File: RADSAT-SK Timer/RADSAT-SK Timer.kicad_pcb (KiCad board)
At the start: 2 copper layers, 90.2 x 95.9 mm, 107 parts, among them J101 Conn_02x26_Odd_Even, J103 Conn_02x26_Odd_Even, J201 Conn_01x07, J202 Conn_01x05, J203 Conn_01x02, J204 Conn_01x02, J205 Conn_01x02, J206 Conn_01x02, J210 ZX62WRD-B-5PC, Q101 IRLML2060, Q102 IRLML2060, Q103 IRLML2060, Q104 IRLML2060, Q105 IRLML2060, Q106 IRLML2060, Q107 IRLML2060, Q108 IRLML2060, Q109 IRLML2060, Q201 IRLML2060, Q202 IRLML2060, SW201 SW_Push, SW202 SW_Push, SW203 SW_Push, SW204 SW_Push, SW205 SW_Push, SW206 SW_Push, U101 LM397MF, U102 LM397MF, U103 LM397MF, U104 CD4052B, U202 LTC3440EMSPBF

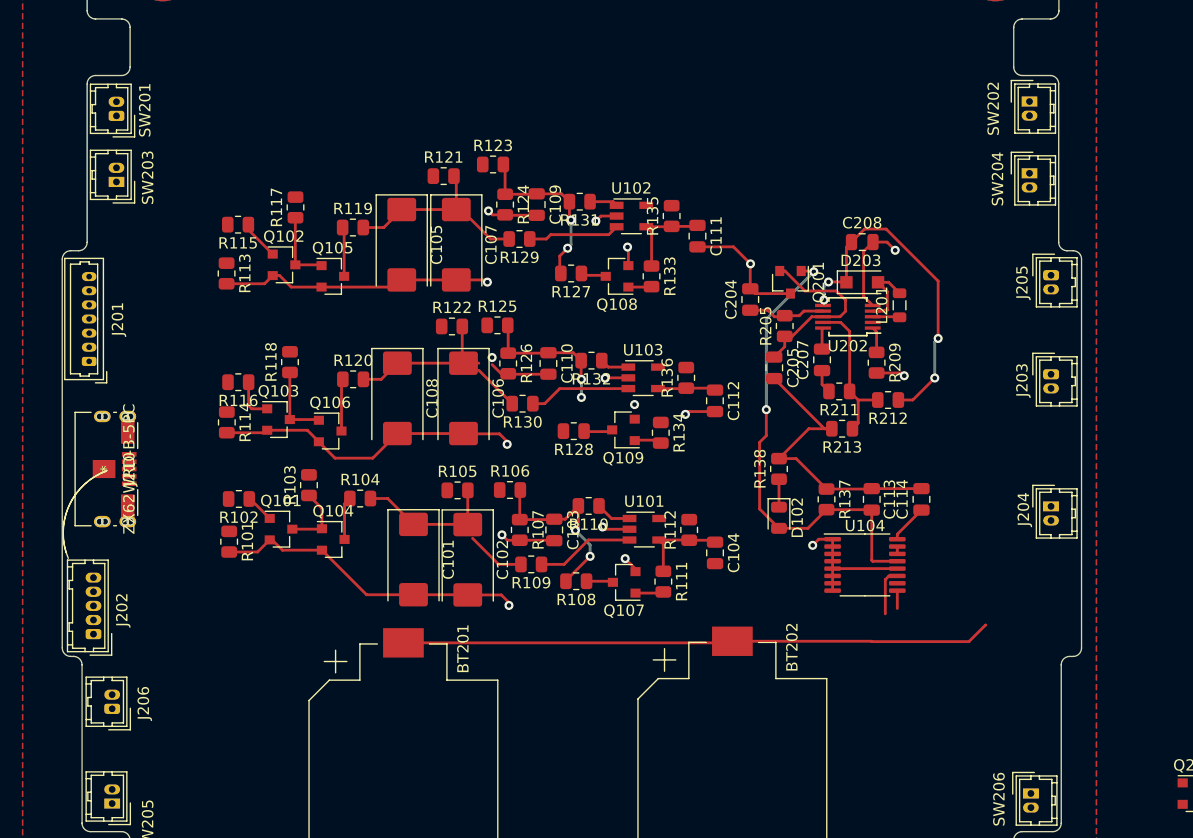
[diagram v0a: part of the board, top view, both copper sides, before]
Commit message: Cleaned Up the USb footprint and updated the libraries to play nice with KiCad
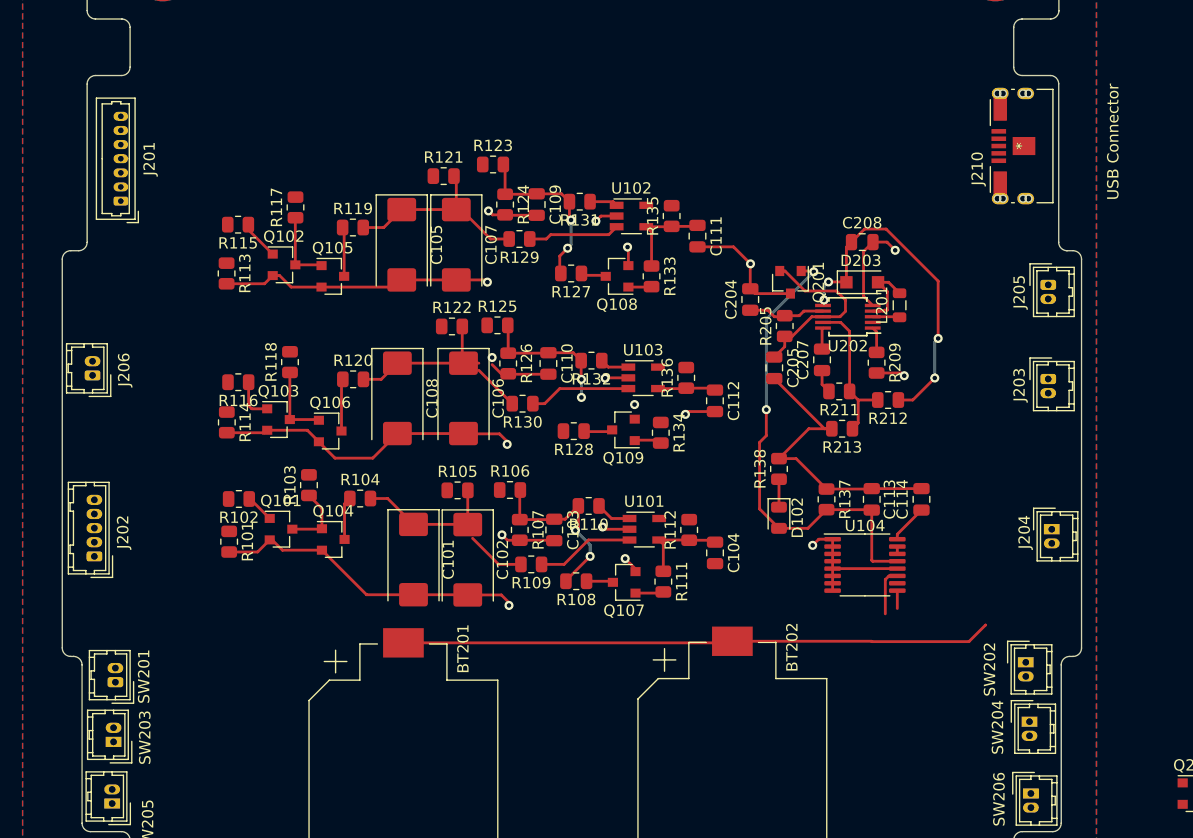
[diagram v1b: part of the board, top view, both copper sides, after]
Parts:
- C205: value C -> 0.1uF
- J210: value ZX62WRD-B-5PC -> USB Connector; footprint ZX62WRD-B-5PC:ZX62WRD-B-5PC -> CONN_ZX62WRD-B-5PC_HIR:CONN_ZX62WRD-B-5PC_HIR
- moved J210 85.9 mm to (119.7, 70.7), turned to 90 degrees
- moved SW201 50.1 mm to (39.5, 118.2)
- moved SW202 49.6 mm to (120.1, 116.4)
- moved SW203 49.5 mm to (39.4, 123.5)
- moved SW204 48.5 mm to (120.4, 121.7)
- moved J206 29.5 mm to (37.5, 91.0)
- moved J201 14.5 mm to (40.0, 75.6)
- moved J202 6.88 mm to (37.7, 107.0)
- moved J204 2.03 mm to (122.4, 104.6)
- moved J205 0.89 mm to (122.0, 83.0)
- moved J203 0.49 mm to (122.0, 91.3)

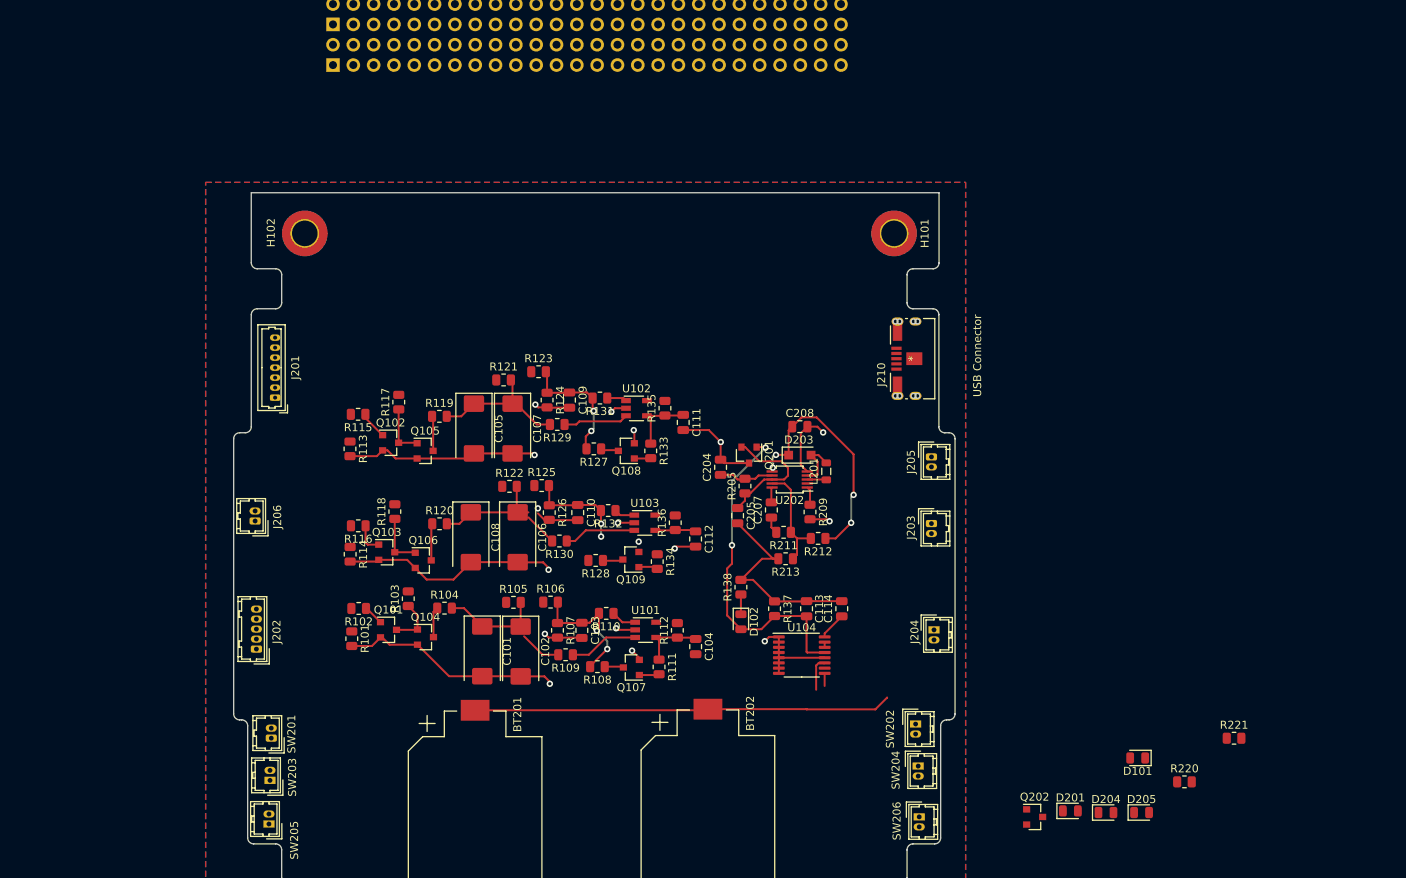
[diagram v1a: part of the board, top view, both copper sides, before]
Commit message: More Library management, added text to pcb to identify easily connectors, Added a cool custom USST RADSAT-SK Logo to the project, may need to be scaled down or placed on back of board
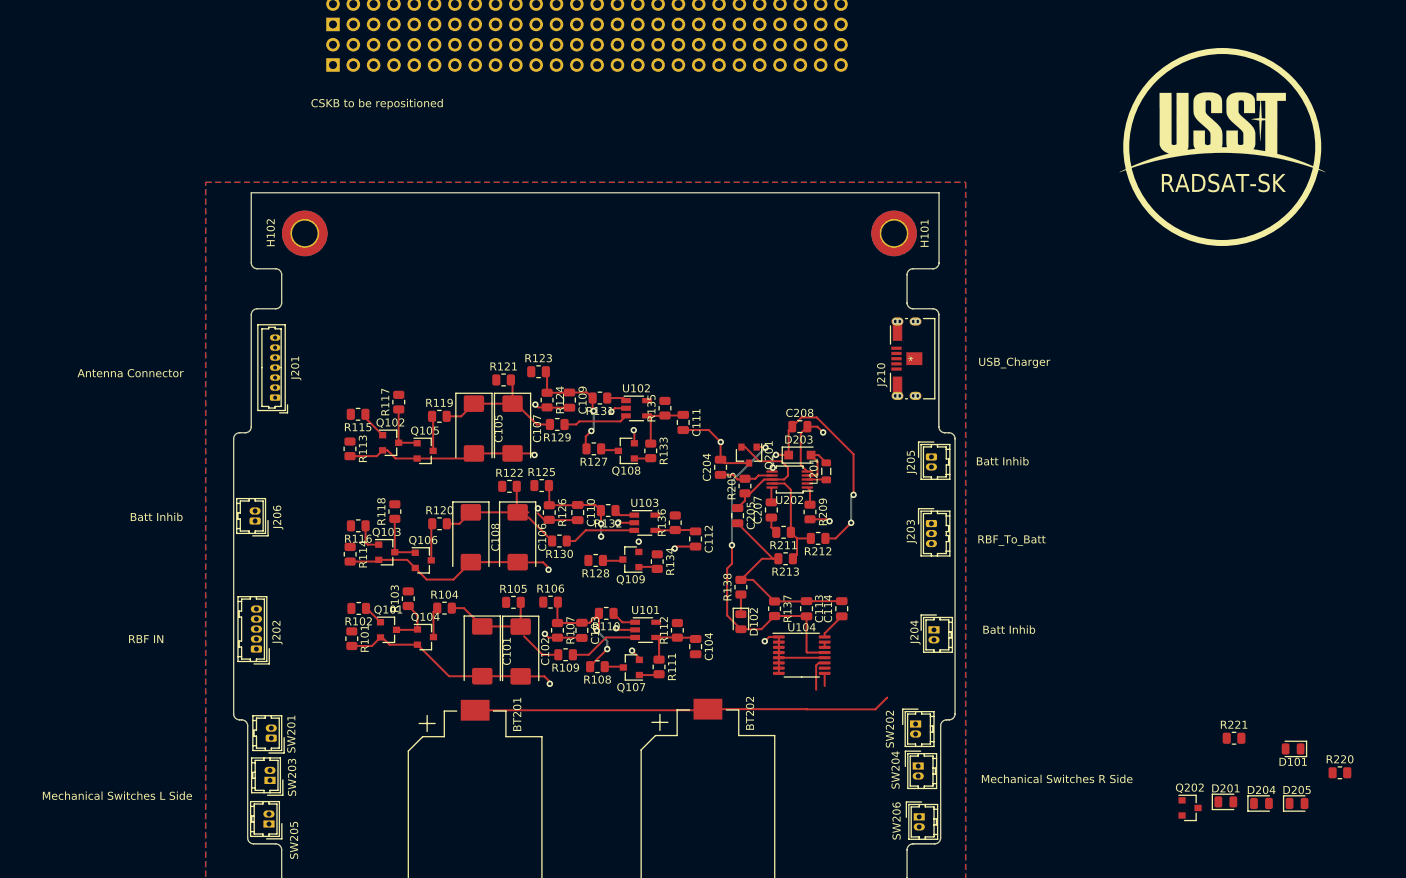
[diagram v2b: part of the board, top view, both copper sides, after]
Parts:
- added G***: LOGO, USSTlogo:USSTLOGO, F.Cu at (158.4, 42.5)
- J203: value Conn_01x02 -> Conn_01x03; footprint Connector_Hirose:Hirose_DF13-02P-1.25DSA_1x02_P1.25mm_Vertical -> Connector_Hirose:Hirose_DF13-03P-1.25DSA_1x03_P1.25mm_Vertical
- J210: value USB Connector -> USB_Charger
- moved D101 19.5 mm to (167.3, 119.5)
- moved D201 19.5 mm to (158.8, 126.1)
- moved D204 19.5 mm to (163.3, 126.3)
- moved Q202 19.5 mm to (154.4, 126.9)
- moved R220 19.5 mm to (173.1, 122.5)
- moved D205 19.5 mm to (167.7, 126.3)
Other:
- board text added: "Antenna Connector"
- board text added: "Batt Inhib"
- board text added: "CSKB to be repositioned"
- board text added: "Mechanical Switches L Side"
- board text added: "Mechanical Switches R Side"
- board text added: "RBF IN"
- board text added: "RBF_To_Batt"

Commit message: JFET
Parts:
- removed G***: LOGO, USSTlogo:USSTLOGO
- added Q203: PJFET, Package_TO_SOT_THT:TO-92L_Inline_Wide, F.Cu at (144.3, 86.4)
- J210: value USB_Charger -> ZX62WRD-B-5PC
- moved Q202 21.6 mm to (138.9, 111.8)
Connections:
- J203 pad 1: Net-(D204-Pad1) -> Net-(J203-Pad1)
- J203 pad 2: GND -> Net-(J203-Pad2)

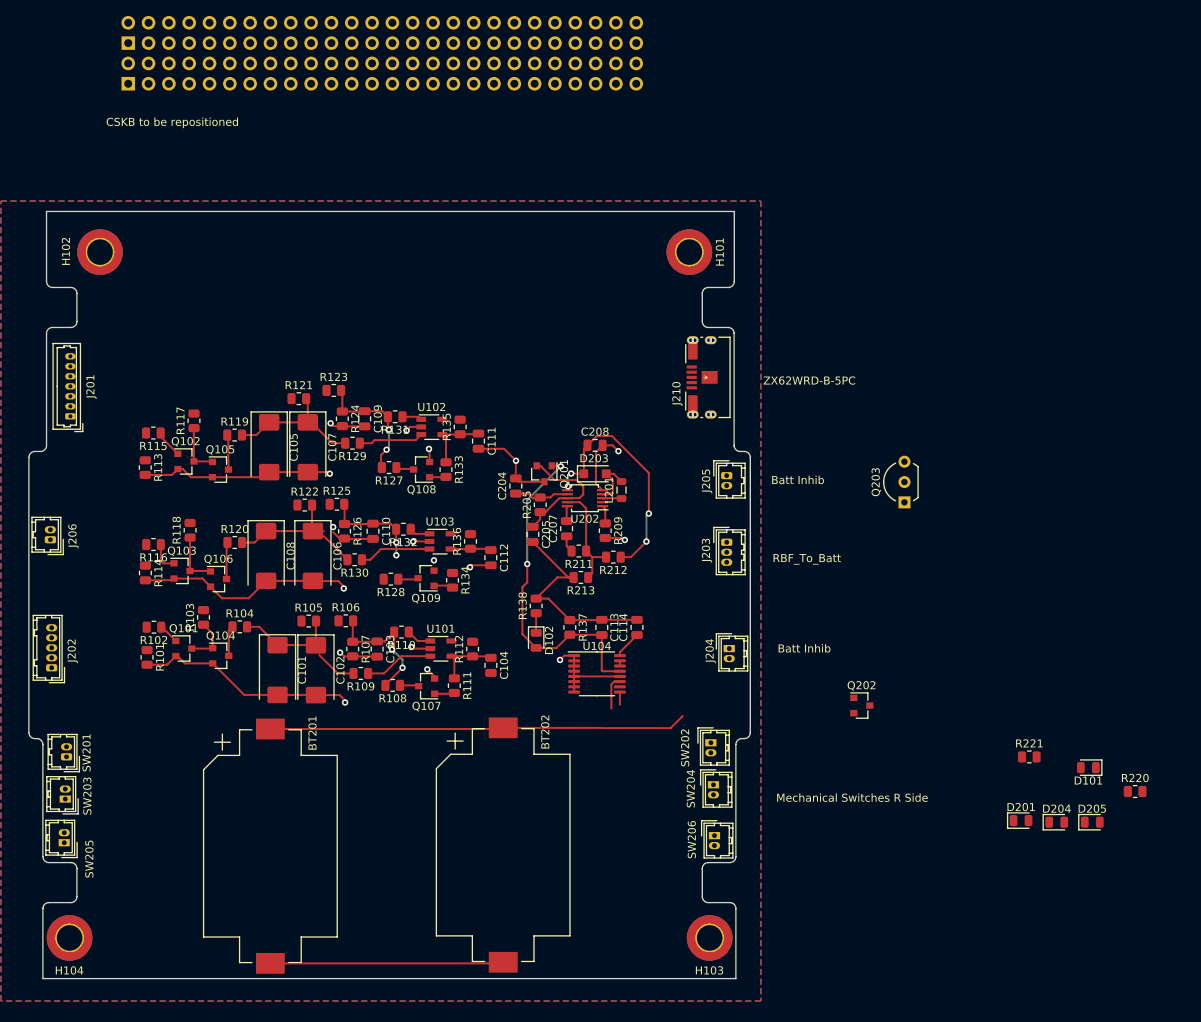
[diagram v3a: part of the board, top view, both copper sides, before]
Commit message: added pchannel JFET and Diode logic for inhibitors, edited the layout a bit still not final
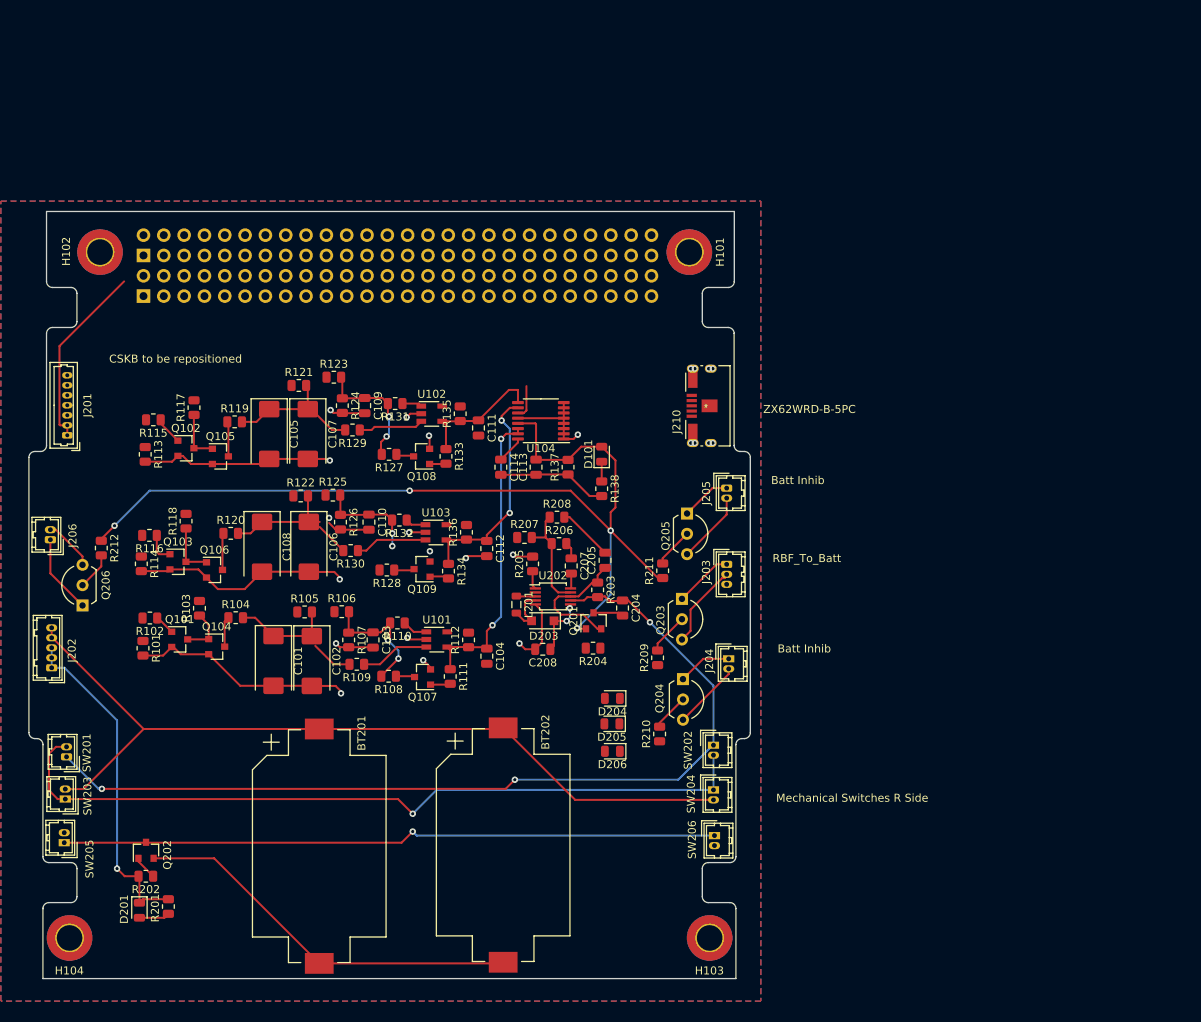
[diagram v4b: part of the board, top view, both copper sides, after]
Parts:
- removed the D101 at (167.3, 119.5)
- added D206: D, Diode_SMD:D_0805_2012Metric, F.Cu at (107.8, 117.5)
- added Q204: PJFET, Package_TO_SOT_THT:TO-92L_Inline_Wide, F.Cu at (116.6, 108.5)
- added Q205: PJFET, Package_TO_SOT_THT:TO-92L_Inline_Wide, F.Cu at (117.1, 87.8)
- added Q206: PJFET, Package_TO_SOT_THT:TO-92L_Inline_Wide, F.Cu at (41.5, 99.3)
- added R204: 100, Resistor_SMD:R_0805_2012Metric, F.Cu at (105.3, 104.6)
- added R209: 100, Resistor_SMD:R_0805_2012Metric, F.Cu at (113.4, 105.8)
- added R210: 100, Resistor_SMD:R_0805_2012Metric, F.Cu at (113.7, 115.3)
- added R211: 100, Resistor_SMD:R_0805_2012Metric, F.Cu at (114.0, 94.9)
- added R212: 100, Resistor_SMD:R_0805_2012Metric, F.Cu at (43.9, 92.1)
- moved R201 121.7 mm to (52.3, 136.9), turned to 270 degrees
- moved R202 111.4 mm to (49.4, 133.1), turned to 180 degrees
- moved D201 110.8 mm to (48.6, 137.4), turned to 270 degrees
- moved Q202 91.3 mm to (49.5, 129.9), turned to 90 degrees
- moved D205 61.3 mm to (107.7, 114.0), turned to 180 degrees
- moved D204 57.7 mm to (107.8, 110.9), turned to 180 degrees
- moved U104 32.4 mm to (98.8, 76.2), turned to 180 degrees
- moved Q203 30.3 mm to (116.5, 98.4), turned to 270 degrees
- moved J101 26.6 mm to (49.1, 55.5)
- moved J103 26.6 mm to (49.1, 60.6)
- moved C208 26.3 mm to (99.1, 104.7), turned to 180 degrees
- moved C114 26.3 mm to (93.8, 82.0), turned to 270 degrees
- moved D101 24.7 mm to (106.4, 80.3), turned to 90 degrees
- moved C113 21.7 mm to (98.2, 82.0), turned to 270 degrees
- moved C204 20.3 mm to (109.0, 99.6), turned to 270 degrees
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- renumbered D102 to D101, R220 to R201, R221 to R202, R205 to R203, R209 to R205, R211 to R206, R212 to R207, R213 to R208
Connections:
- D205 pad 2: BUS_EN -> +5V
- J101 pad 26: Net-(D101-Pad2) -> +5V
- J204 pad 1: BUS_EN -> Net-(J204-Pad1)
- J204 pad 2: GND -> Net-(J204-Pad2)
- J205 pad 1: BUS_EN -> Net-(J205-Pad1)
- J205 pad 2: GND -> Net-(J205-Pad2)
- J206 pad 1: BUS_EN -> Net-(J206-Pad1)
- J206 pad 2: GND -> Net-(J206-Pad2)
- Q201 pad 1: BUS_EN -> Net-(Q201-Pad1)
- Q203 pad 2: Net-(D204-Pad1) -> Net-(Q203-Pad2)
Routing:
- net Net-(C204-Pad1): track 6.88 -> 114.9 mm, vias 0 -> 3
- net Net-(SW201-Pad2): track 0.00 -> 97.0 mm, vias 0 -> 1
- net Net-(Q202-Pad3): track 0.00 -> 82.1 mm, vias 0 -> 1
- net BUS_EN: track 42.2 -> 119.7 mm, vias 2 -> 4
- net Net-(BT201-Pad1): track 52.2 -> 105.5 mm
- net Net-(D201-Pad1): track 0.00 -> 42.2 mm, vias 0 -> 1
- net Timer_A_out: track 8.59 -> 37.9 mm, vias 0 -> 2
- net +3V3: track 0.00 -> 23.5 mm
- net Timer_C_out: track 5.18 -> 28.0 mm, vias 0 -> 2
- net +BATT: track 38.2 -> 15.4 mm, vias 4 -> 2
- net Net-(BT201-Pad2): track 29.7 -> 49.2 mm
- net Net-(J203-Pad2): track 0.00 -> 10.6 mm
- net Net-(J206-Pad1): track 0.00 -> 9.89 mm
- net GND: track 166.6 -> 157.1 mm, vias 17 -> 16
- net Net-(J205-Pad2): track 0.00 -> 9.06 mm
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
